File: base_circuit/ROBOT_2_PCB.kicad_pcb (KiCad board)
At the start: 2 copper layers, 20 parts, among them J1 Conn_01x04, J2 Output_Supply, J3 Conn_01x01_Female, J4 M1,2, J5 M3,4, M1 Conn_01x04_Female, M2 Conn_01x04_Female, M3 Conn_01x04_Female, M4 Conn_01x04_Female, SW2 SW_SPDT

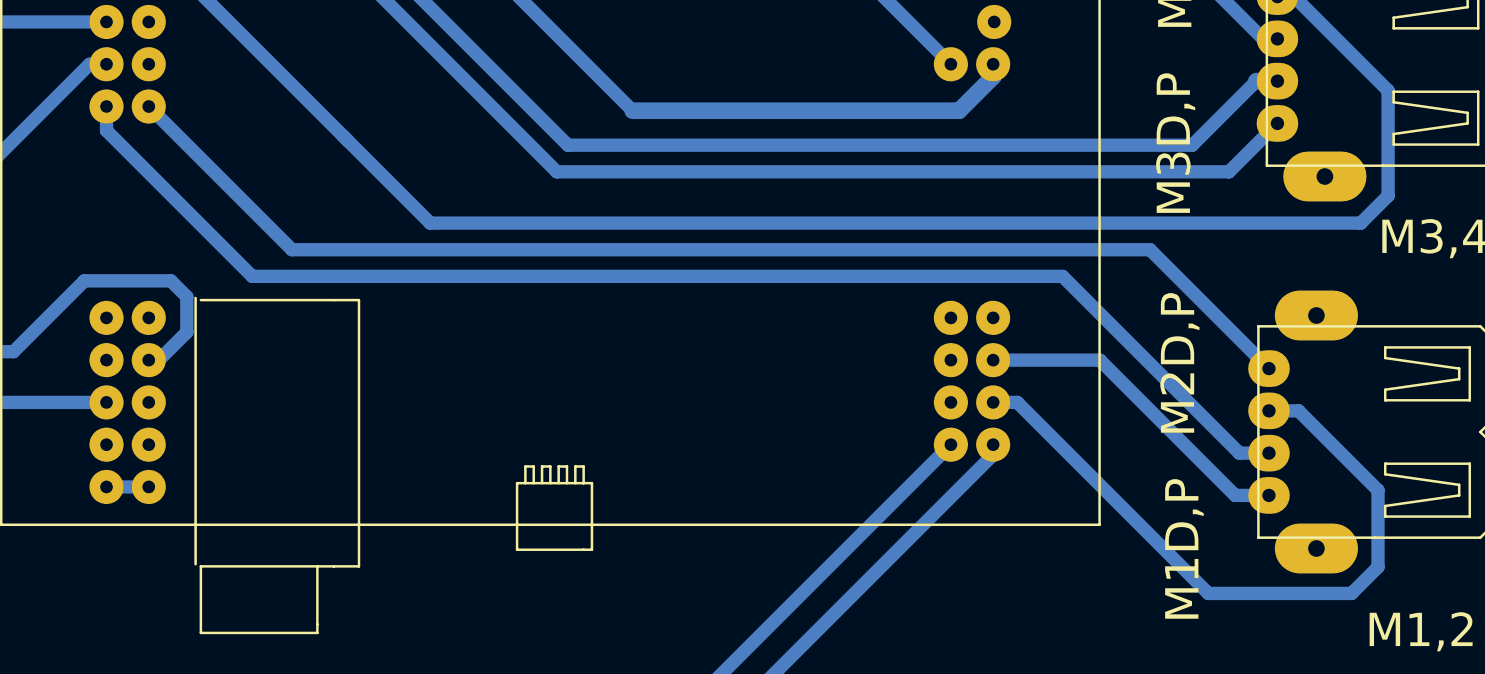
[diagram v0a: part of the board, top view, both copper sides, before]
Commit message: Add ioc file od base circuit
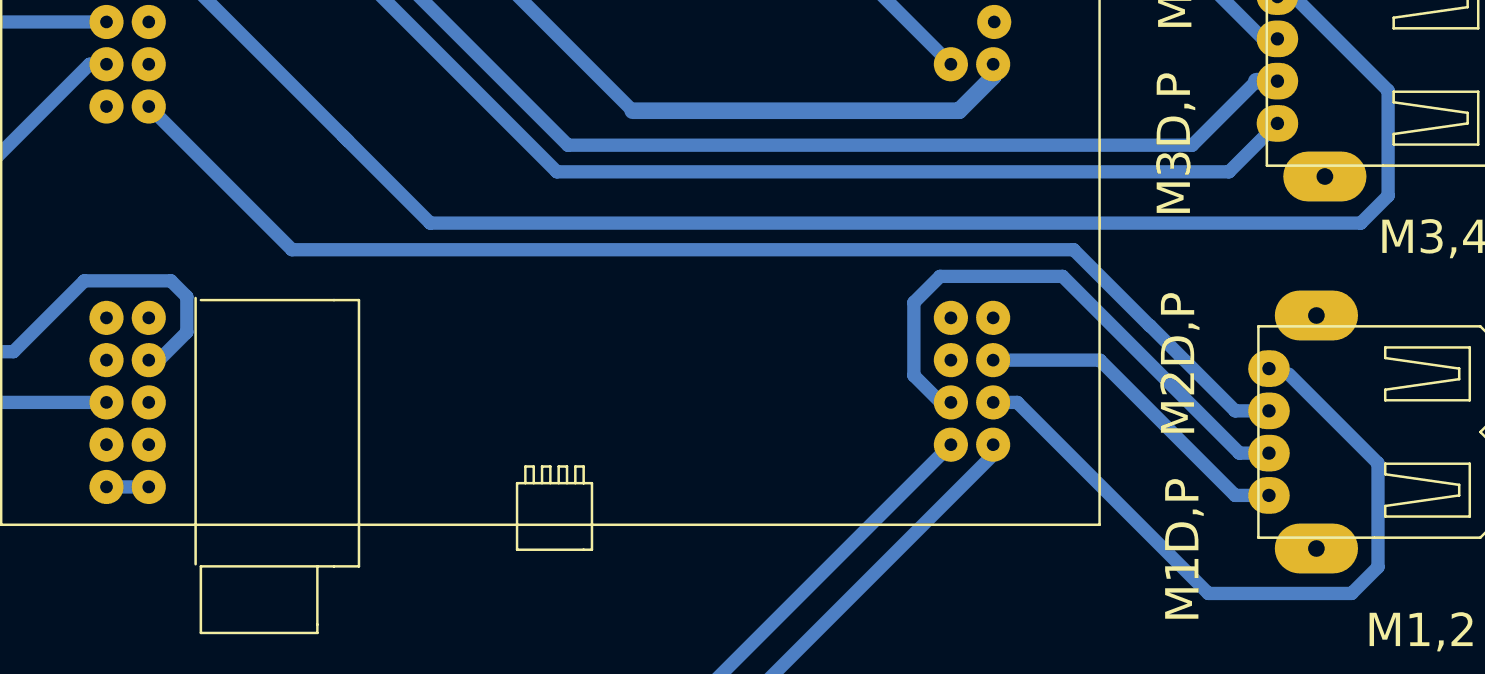
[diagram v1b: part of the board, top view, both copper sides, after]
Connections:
- S1 pad 31: Motor_1_Pwm -> unconnected-(S1-Pad31)
- S1 pad 32: Motor_2_Pwm -> M2D
- S1 pad 78: FW1_E2 -> unconnected-(S1-Pad78)
- S1 pad 95: unconnected-(S1-Pad95) -> Motor_1_Pwm
- S1 pad 96: M2D -> Motor_2_Pwm
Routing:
- net Motor_1_Pwm: track 79.3 -> 33.7 mm
- net M2D: track 41.7 -> 74.9 mm
- net Motor_2_Pwm: track 73.8 -> 42.3 mm
- net unconnected-(S1-Pad50): track 0.00 -> 2.54 mm
- net 5V: track 344.9 -> 342.4 mm

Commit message: Final design and add Pin Hole Size in  driLL_siZE.txt file
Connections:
- J1 pad 1: Net-(J1-Pad1) -> 5V
- J1 pad 2: Net-(J1-Pad2) -> 5V
- J1 pad 4: 5V -> GND
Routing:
- net unconnected-(S1-Pad50): track 2.54 -> 0.00 mm
- net SDA: track 54.6 -> 53.1 mm
- net 5V: track 342.4 -> 343.6 mm

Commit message: Final Edit of base circuit
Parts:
- moved J4 5.80 mm to (158.5, 143.8)
- moved C2 5.28 mm to (148.6, 102.1)
- moved IMU1 5.28 mm to (158.2, 102.4)
- moved J5 5.28 mm to (159.0, 119.1)
- moved D3 5.28 mm to (159.0, 87.9)
- moved J2 5.28 mm to (150.8, 62.5)
- moved MPU1 5.28 mm to (148.8, 87.4)
- moved M2 2.92 mm to (45.9, 132.2)
- moved C3 2.92 mm to (40.8, 87.4)
- moved D2 2.92 mm to (62.9, 73.7)
- moved POW_SPLY1 2.92 mm to (47.0, 63.9)
- moved SW2 2.92 mm to (50.4, 78.7)
- moved J1 2.92 mm to (47.7, 91.2)
- moved J3 2.92 mm to (48.2, 112.0)
- moved M1 2.92 mm to (58.6, 132.3)
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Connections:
- S1 pad 50: unconnected-(S1-Pad50) -> GND
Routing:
- net GND: track 23.4 -> 182.8 mm
- net 3.3V: track 141.9 -> 150.9 mm
- net SDA: track 53.1 -> 61.3 mm
- net Motor_2_Pwm: track 42.3 -> 50.2 mm
- net M2D: track 74.9 -> 81.2 mm
- net M1D: track 19.9 -> 26.2 mm
- net Motor_1_Pwm: track 33.7 -> 39.9 mm
- net 5V: track 343.6 -> 349.5 mm
- net Motor_3_Pwm: track 79.8 -> 85.2 mm
- net M3D: track 77.0 -> 82.2 mm
- net Motor_4_Pwm: track 116.0 -> 121.2 mm
- net M4D: track 18.6 -> 23.7 mm
- net SCL: track 50.9 -> 56.0 mm
- net TX: track 115.4 -> 120.2 mm
- net Motor_2_Enc_1: track 62.9 -> 66.1 mm
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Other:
- board text added: "ABU ROBOCON 2023"
- board text added: "BASE"
- board text added: "D->P"
- board text added: "RJN"
- board text removed: "A"
- board text removed: "M1D,P"
- board text removed: "M2D,P"
- board text removed: "M3D,P"
- board text removed: "M4D,P"
- board text removed: "P"
- board text removed: "ROBOCON 2023"

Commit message: Final Designgit add base_circuit/git add base_circuit/
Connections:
- SW2 pad : (no net) -> RX
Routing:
- net GND: track 182.8 -> 497.5 mm
- net 5V: track 349.5 -> 351.4 mm
- net RX: track 125.9 -> 125.2 mm
- net SDA: track 61.3 -> 60.7 mm
